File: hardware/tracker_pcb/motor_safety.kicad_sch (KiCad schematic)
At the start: 3 parts, among them U1 SN74AUP2G125YZPR, U2 SN74AUP2G125YZPR

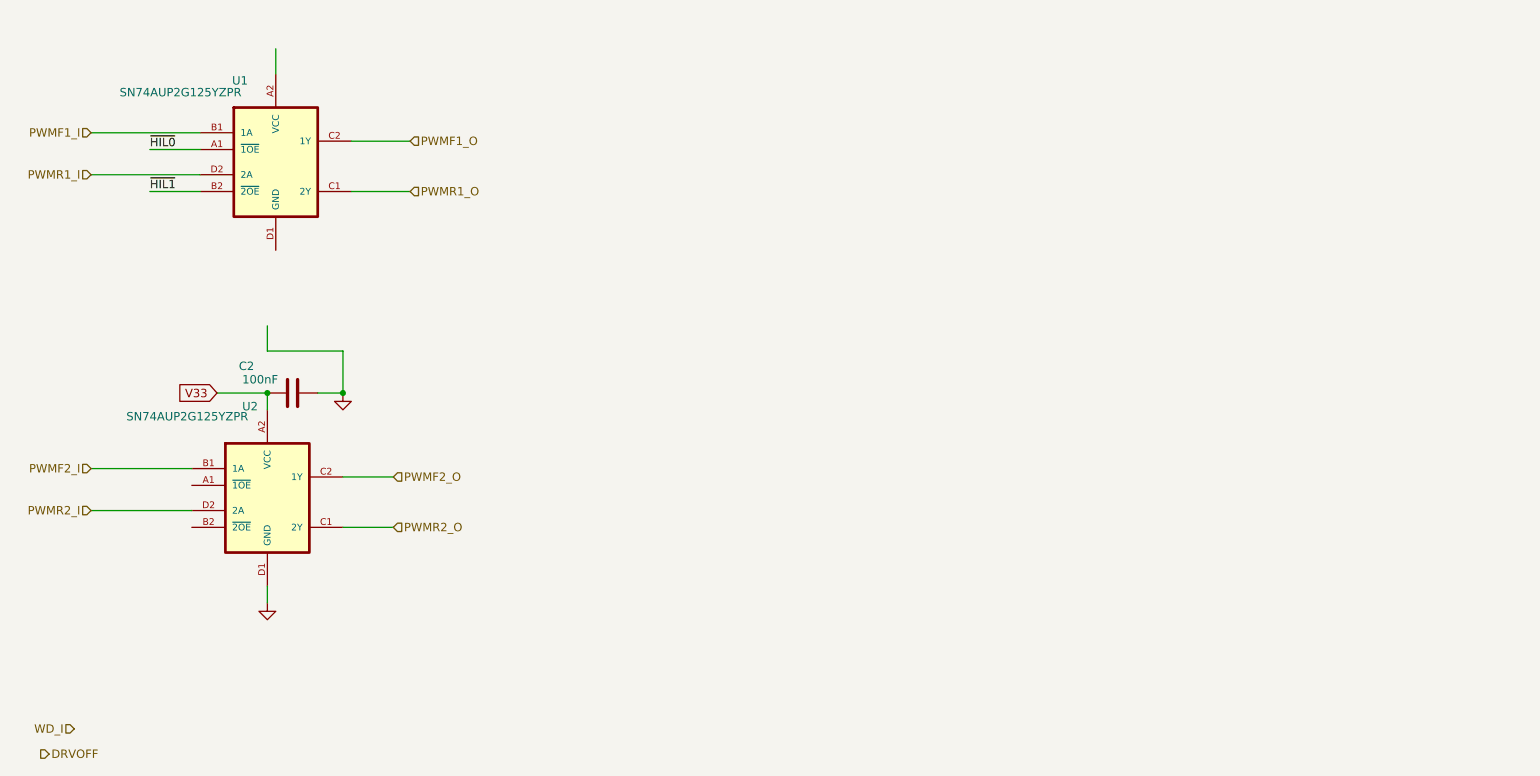
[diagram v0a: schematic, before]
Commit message: more motor safety
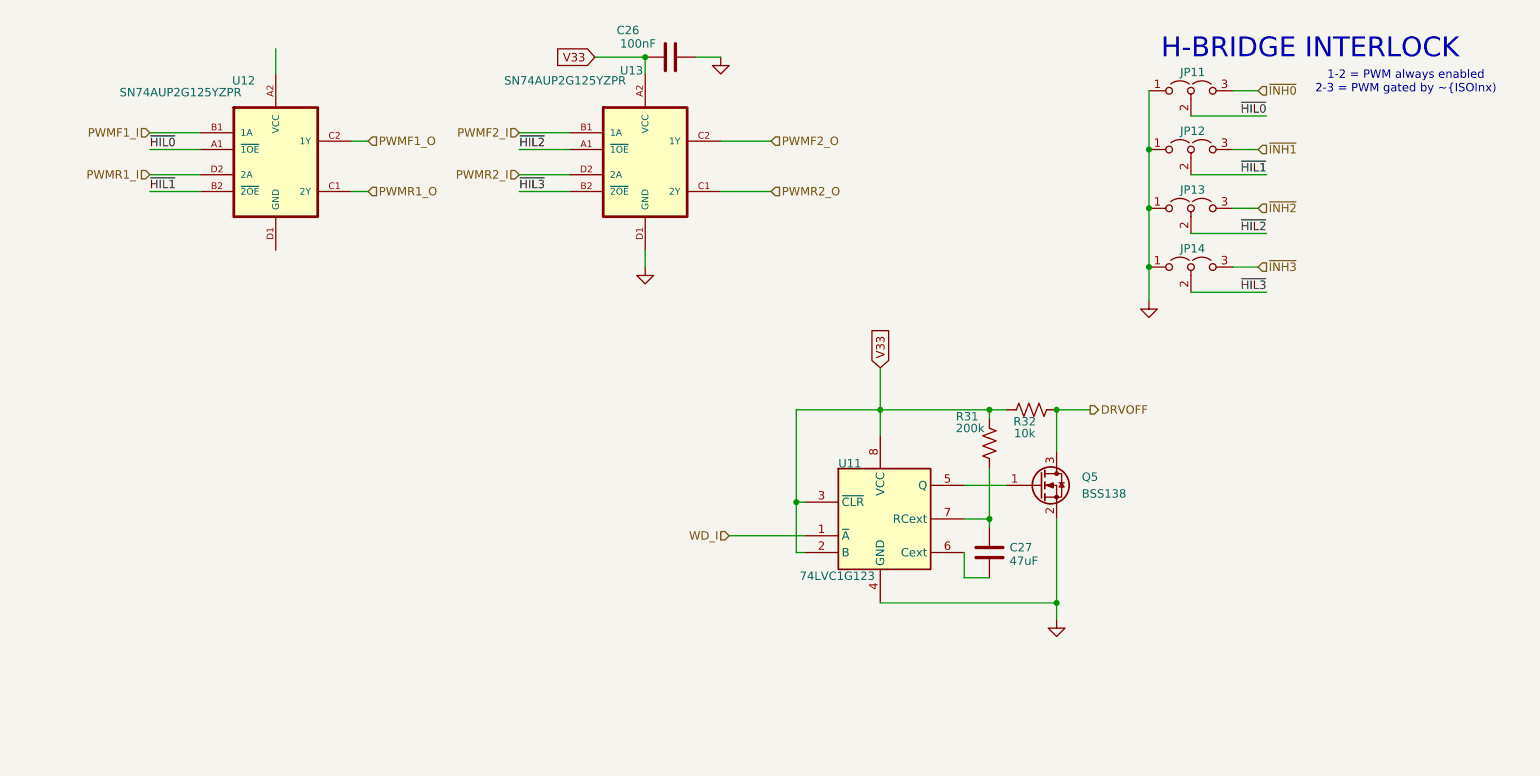
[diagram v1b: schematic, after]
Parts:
- added C27: 47uF, Capacitor_SMD:C_0805_2012Metric, symbol Device:C
- added JP11, JP12, JP13, JP14: Jumper_3_Open, Connector_PinHeader_2.00mm:PinHeader_1x03_P2.00mm_Vertical, symbol Jumper:Jumper_3_Open
- added Q5: BSS138, Package_TO_SOT_SMD:SOT-23, symbol Transistor_FET:BSS138
- added R31: 200k, Resistor_SMD:R_0603_1608Metric, symbol Device:R_US
- added R32: 10k, Resistor_SMD:R_0603_1608Metric, symbol Device:R_US
- added U11: 74LVC1G123, footprint:74LVC1G123GN115, symbol symbol:74LVC1G123
- renumbered C2 to C26, U1 to U12, U2 to U13
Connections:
- net DRVOFF: now also Q5.3 (D), R32.1
- net GND: now also JP11.1 (A), JP12.1 (A), JP13.1 (A), JP14.1 (A), Q5.2 (S), U11.4 (GND)
- net V33: now also R31.2, R32.2, U11.2 (B), U11.3 (~{CLR}), U11.8 (VCC)
- net WD_I: now also U11.1 (~{A})
- net ~{HIL0}: now also JP11.2 (C)
- net ~{HIL1}: now also JP12.2 (C)
- net ~{HIL2}: now reaches U13.A1 (~{1OE})
- net ~{HIL2}: now also JP13.2 (C)
- net ~{HIL3}: now reaches U13.B2 (~{2OE})
- net ~{HIL3}: now also JP14.2 (C)
- new net: C27.1, R31.1, U11.7 (RCext)
- new net: C27.2, U11.6 (Cext)
- new net: Q5.1 (G), U11.5 (Q)
- new net ~{INH0}: JP11.3 (B)
- new net ~{INH1}: JP12.3 (B)
- new net ~{INH2}: JP13.3 (B)
- new net ~{INH3}: JP14.3 (B)
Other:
- note added: "1-2 = PWM always enabled 2-3 = PWM gated by ~{ISOInx)"
- note added: "H-BRIDGE INTERLOCK"
- moved on the sheet: C26, U13

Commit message: Motor safety edits
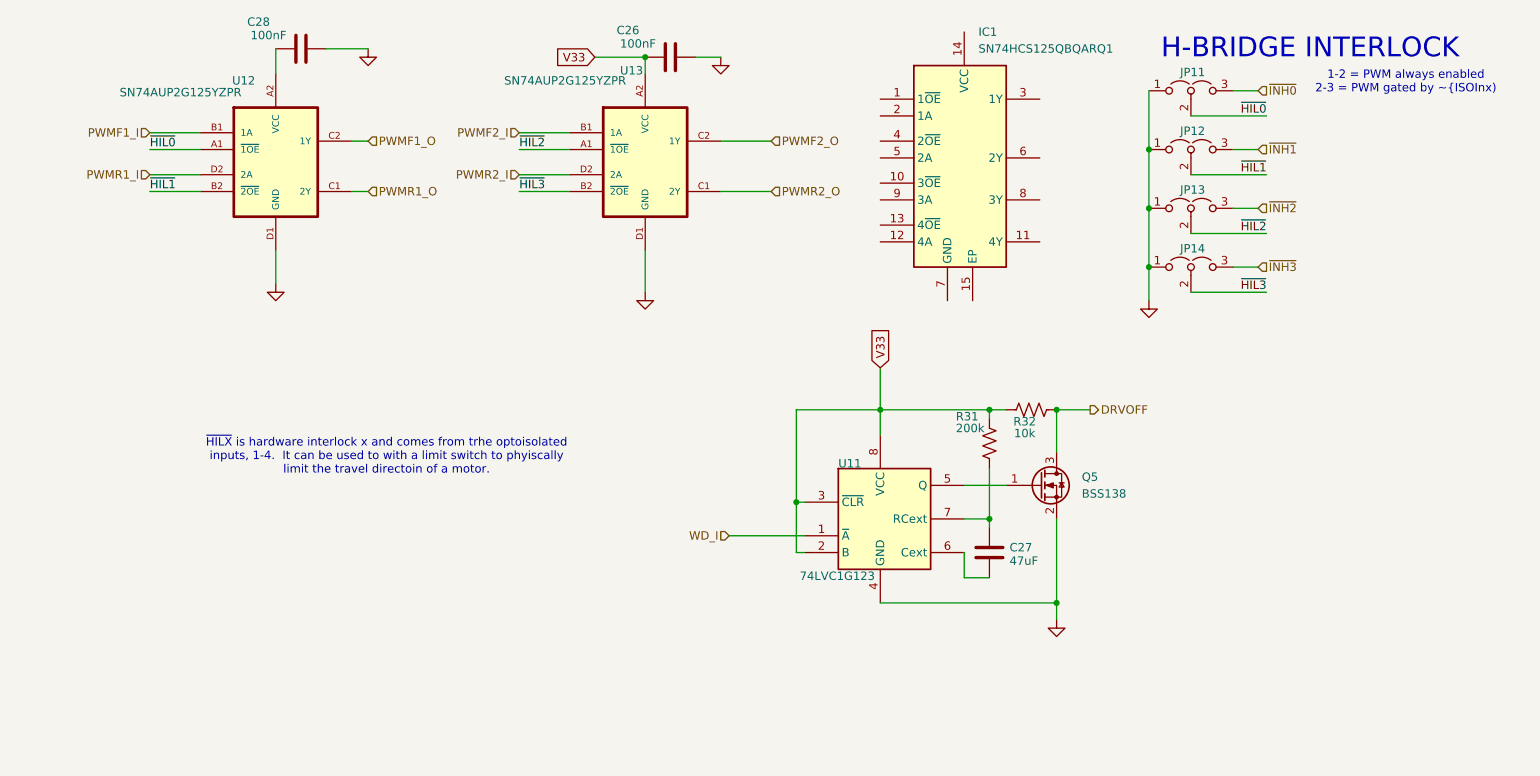
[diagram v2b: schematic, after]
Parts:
- added C28: 100nF, Capacitor_SMD:C_0603_1608Metric, symbol Device:C
- added IC1: SN74HCS125QBQARQ1, footprint:SN74HCS125QBQARQ1, symbol symbol:SN74HCS125QBQARQ1
- C27: LCSC (none) -> C77072
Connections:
- net GND: now also U12.D1 (GND), C28.2
- net at U12.A2 (VCC): now also C28.1
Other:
- note added: "~{HILX} is hardware interlock x and comes from trhe optoisolated inputs, 1-4. It can be used to with a limit switch to phyiscally limit the travel directoin of a motor."
